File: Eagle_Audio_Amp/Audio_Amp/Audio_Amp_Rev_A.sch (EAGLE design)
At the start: 14 parts, among them IC1 LM386M-1

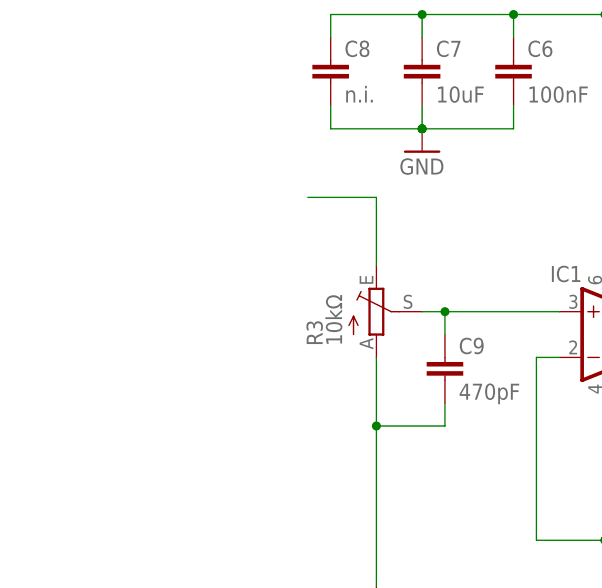
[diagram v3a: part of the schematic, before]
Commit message: Add stereo audio jack
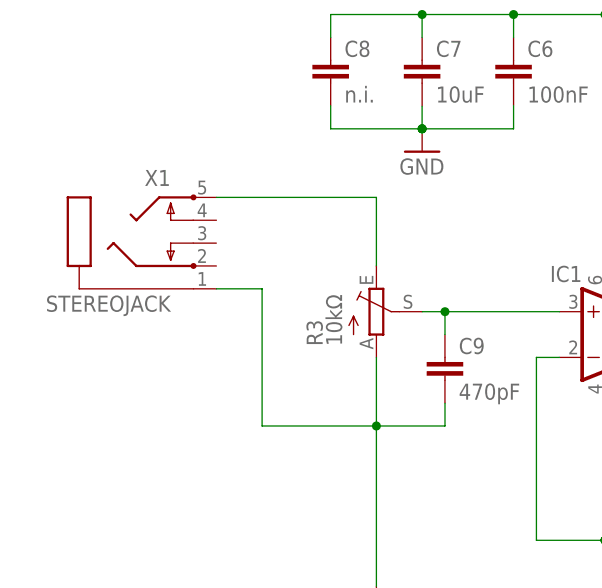
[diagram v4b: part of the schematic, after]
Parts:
- added X1: STEREOJACK, adafruit:STEREOJACK
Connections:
- net GND: now also X1.1
- net N$8: now also X1.5
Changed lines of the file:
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@@
 <layer number="48" name="Document" color="7" fill="1" visible="no" active="no"/>
 <layer number="49" name="Reference" color="7" fill="1" visible="no" active="no"/>
+<layer number="50" name="dxf" color="7" fill="1" visible="no" active="no"/>
 <layer number="51" name="tDocu" color="6" fill="1" visible="no" active="no"/>
 <layer number="52" name="bDocu" color="7" fill="1" visible="no" active="no"/>
+<layer number="53" name="tGND_GNDA" color="7" fill="9" visible="no" active="no"/>
+<layer number="54" name="bGND_GNDA" color="1" fill="9" visible="no" active="no"/>
+<layer number="56" name="wert" color="7" fill="1" visible="no" active="no"/>
+<layer number="57" name="tCAD" color="7" fill="1" visible="no" active="no"/>
+<layer number="59" name="tCarbon" color="7" fill="1" visible="no" active="no"/>
+<layer number="60" name="bCarbon" color="7" fill="1" visible="no" active="no"/>
 <layer number="90" name="Modules" color="5" fill="1" visible="yes" active="yes"/>
 <layer number="91" name="Nets" color="2" fill="1" visible="yes" active="yes"/>
@@
 <layer number="97" name="Info" color="7" fill="1" visible="yes" active="yes"/>
 <layer number="98" name="Guide" color="6" fill="1" visible="yes" active="yes"/>
+<layer number="99" name="SpiceOrder" color="7" fill="1" visible="no" active="no"/>
+<layer number="100" name="Muster" color="7" fill="1" visible="no" active="no"/>
+<layer number="101" name="Patch_Top" color="12" fill="4" visible="no" active="yes"/>
+<layer number="102" name="Vscore" color="7" fill="1" visible="no" active="yes"/>
+<layer number="103" name="fp3" color="7" fill="1" visible="no" active="yes"/>
+<layer number="104" name="Name" color="7" fill="1" visible="no" active="yes"/>
+<layer number="105" name="Beschreib" color="9" fill="1" visible="no" active="yes"/>
+<layer number="106" name="BGA-Top" color="4" fill="1" visible="no" active="yes"/>
+<layer number="107" name="BD-Top" color="5" fill="1" visible="no" active="yes"/>
+<layer number="108" name="fp8" color="7" fill="1" visible="no" active="yes"/>
+<layer number="109" name="fp9" color="7" fill="1" visible="no" active="yes"/>
+<layer number="110" name="fp0" color="7" fill="1" visible="no" active="yes"/>
+<layer number="111" name="LPC17xx" color="7" fill="1" visible="no" active="yes"/>
+<layer number="112" name="tSilk" color="7" fill="1" visible="no" active="yes"/>
+<layer number="113" name="ReferenceLS" color="7" fill="1" visible="no" active="no"/>
+<layer number="116" name="Patch_BOT" color="9" fill="4" visible="no" active="yes"/>
+<layer number="118" name="Rect_Pads" color="7" fill="1" visible="no" active="no"/>
+<layer number="121" name="_tsilk" color="7" fill="1" visible="no" active="yes"/>
+<layer number="122" name="_bsilk" color="7" fill="1" visible="no" active="yes"/>
+<layer number="123" name="tTestmark" color="7" fill="1" visible="no" active="yes"/>
+<layer number="124" name="bTestmark" color="7" fill="1" visible="no" active="yes"/>
+<layer number="125" name="_tNames" color="7" fill="1" visible="no" active="yes"/>
+<layer number="126" name="_bNames" color="7" fill="1" visible="no" active="yes"/>
+<layer number="127" name="_tValues" color="7" fill="1" visible="no" active="yes"/>
+<layer number="128" name="_bValues" color="7" fill="1" visible="no" active="yes"/>
+<layer number="129" name="Mask" color="7" fill="1" visible="yes" active="yes"/>
+<layer number="131" name="tAdjust" color="7" fill="1" visible="no" active="yes"/>
+<layer number="132" name="bAdjust" color="7" fill="1" visible="no" active="yes"/>
+<layer number="144" name="Drill_legend" color="7" fill="1" visible="no" active="yes"/>
+<layer number="150" name="Notes" color="7" fill="1" visible="no" active="yes"/>
+<layer number="151" name="HeatSink" color="7" fill="1" visible="no" active="yes"/>
+<layer number="152" name="_bDocu" color="7" fill="1" visible="no" active="yes"/>
+<layer number="153" name="FabDoc1" color="6" fill="1" visible="no" active="no"/>
+<layer number="154" name="FabDoc2" color="2" fill="1" visible="no" active="no"/>
+<layer number="155" name="FabDoc3" color="7" fill="15" visible="no" active="no"/>
+<layer number="199" name="Contour" color="7" fill="1" visible="no" active="yes"/>
+<layer number="200" name="200bmp" color="1" fill="10" visible="no" active="yes"/>
+<layer number="201" name="201bmp" color="2" fill="1" visible="no" active="no"/>
+<layer number="202" name="202bmp" color="3" fill="1" visible="no" active="no"/>
+<layer number="203" name="203bmp" color="4" fill="10" visible="no" active="yes"/>
+<layer number="204" name="204bmp" color="5" fill="10" visible="no" active="yes"/>
+<layer number="205" name="205bmp" color="6" fill="10" visible="no" active="yes"/>
+<layer number="206" name="206bmp" color="7" fill="10" visible="no" active="yes"/>
+<layer number="207" name="207bmp" color="8" fill="10" visible="no" active="yes"/>
+<layer number="208" name="208bmp" color="9" fill="10" visible="no" active="yes"/>
+<layer number="209" name="209bmp" color="7" fill="1" visible="no" active="yes"/>
+<layer number="210" name="210bmp" color="7" fill="1" visible="no" active="yes"/>
+<layer number="211" name="211bmp" color="7" fill="1" visible="no" active="yes"/>
+<layer number="212" name="212bmp" color="7" fill="1" visible="no" active="yes"/>
+<layer number="213" name="213bmp" color="7" fill="1" visible="no" active="yes"/>
+<layer number="214" name="214bmp" color="7" fill="1" visible="no" active="yes"/>
+<layer number="215" name="215bmp" color="7" fill="1" visible="no" active="yes"/>
+<layer number="216" name="216bmp" color="7" fill="1" visible="no" active="yes"/>
+<layer number="217" name="217bmp" color="18" fill="1" visible="no" active="no"/>
+<layer number="218" name="218bmp" color="19" fill="1" visible="no" active="no"/>
+<layer number="219" name="219bmp" color="20" fill="1" visible="no" active="no"/>
+<layer number="220" name="220bmp" color="21" fill="1" visible="no" active="no"/>
+<layer number="221" name="221bmp" color="22" fill="1" visible="no" active="no"/>
+<layer number="222" name="222bmp" color="23" fill="1" visible="no" active="no"/>
+<layer number="223" name="223bmp" color="24" fill="1" visible="no" active="no"/>
+<layer number="224" name="224bmp" color="25" fill="1" visible="no" active="no"/>
+<layer number="225" name="225bmp" color="7" fill="1" visible="yes" active="yes"/>
+<layer number="226" name="226bmp" color="7" fill="1" visible="yes" active="yes"/>
+<layer number="227" name="227bmp" color="7" fill="1" visible="yes" active="yes"/>
+<layer number="228" name="228bmp" color="7" fill="1" visible="yes" active="yes"/>
+<layer number="229" name="229bmp" color="7" fill="1" visible="yes" active="yes"/>
+<layer number="230" name="230bmp" color="7" fill="1" visible="yes" active="yes"/>
+<layer number="231" name="Eagle3D_PG1" color="7" fill="1" visible="no" active="no"/>
+<layer number="232" name="Eagle3D_PG2" color="7" fill="1" visible="no" active="no"/>
+<layer number="233" name="Eagle3D_PG3" color="7" fill="1" visible="no" active="no"/>
+<layer number="248" name="Housing" color="7" fill="1" visible="no" active="yes"/>
+<layer number="249" name="Edge" color="7" fill="1" visible="no" active="yes"/>
+<layer number="250" name="Descript" color="7" fill="1" visible="no" active="no"/>
+<layer number="251" name="SMDround" color="7" fill="1" visible="no" active="no"/>
+<layer number="254" name="cooling" color="7" fill="1" visible="no" active="yes"/>
+<layer number="255" name="routoute" color="7" fill="1" visible="yes" active="yes"/>
 </layers>
 <schematic xreflabel="%F%N/%S.%C%R" xrefpart="/%S.%C%R">
@@
 <part name="SP1" library="speaker" deviceset="SMS-1308MS-2-R" device=""/>
 <part name="GND5" library="supply1" deviceset="GND" device=""/>
+<part name="X1" library="adafruit" deviceset="STEREOJACK" device=""/>
 </parts>
 <sheets>
@@
 <instance part="SP1" gate="A" x="144.78" y="40.64"/>
 <instance part="GND5" gate="1" x="144.78" y="25.4"/>
+<instance part="X1" gate="1" x="33.02" y="68.58" rot="MR0"/>
 </instances>
 <busses>
@@
 <wire x1="71.12" y1="45.72" x2="63.5" y2="45.72" width="0.1524" layer="91"/>
 <junction x="63.5" y="45.72"/>
+<pinref part="X1" gate="1" pin="1"/>
+<wire x1="45.72" y1="60.96" x2="50.8" y2="60.96" width="0.1524" layer="91"/>
+<wire x1="50.8" y1="60.96" x2="50.8" y2="45.72" width="0.1524" layer="91"/>
+<wire x1="50.8" y1="45.72" x2="63.5" y2="45.72" width="0.1524" layer="91"/>
 </segment>
 <segment>
@@
 <pinref part="R3" gate="1" pin="E"/>
 <wire x1="63.5" y1="63.5" x2="63.5" y2="71.12" width="0.1524" layer="91"/>
-<wire x1="63.5" y1="71.12" x2="55.88" y2="71.12" width="0.1524" layer="91"/>
-</segment>
-</net>
+<pinref part="X1" gate="1" pin="5"/>
+<wire x1="45.72" y1="71.12" x2="63.5" y2="71.12" width="0.1524" layer="91"/>
+</segment>
+</net>

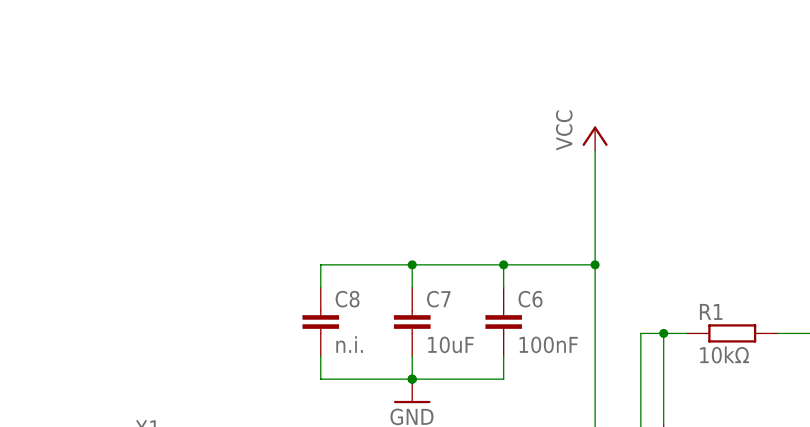
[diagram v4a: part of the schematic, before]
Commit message: Add USB micro B connector for power
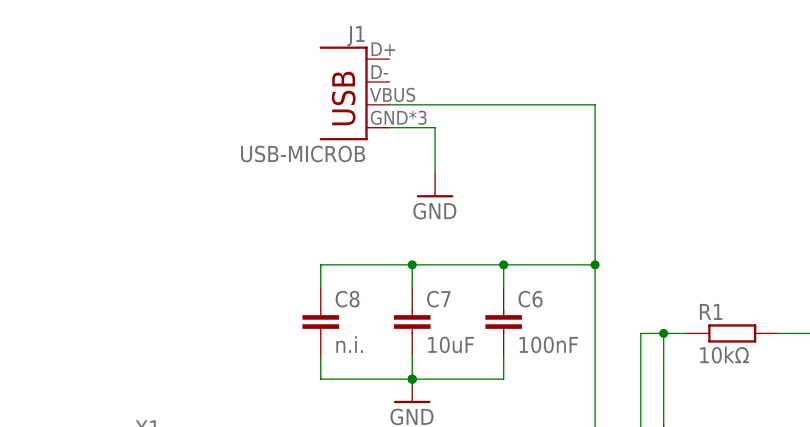
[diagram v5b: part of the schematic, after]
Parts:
- added J1: USB-MICROB, SparkFun-Connectors:USB-MICROB
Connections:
- removed net VCC: C6.1, C7.1, C8.1, IC1.VS
- new net N$10: C6.1, C7.1, C8.1, IC1.VS, J1.VBUS
- net GND: now also J1.GND
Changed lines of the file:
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@@
 <layer number="112" name="tSilk" color="7" fill="1" visible="no" active="yes"/>
 <layer number="113" name="ReferenceLS" color="7" fill="1" visible="no" active="no"/>
+<layer number="114" name="Badge_Outline" color="7" fill="1" visible="yes" active="yes"/>
+<layer number="115" name="ReferenceISLANDS" color="7" fill="1" visible="yes" active="yes"/>
 <layer number="116" name="Patch_BOT" color="9" fill="4" visible="no" active="yes"/>
 <layer number="118" name="Rect_Pads" color="7" fill="1" visible="no" active="no"/>
@@
 <part name="GND1" library="supply1" deviceset="GND" device=""/>
 <part name="GND2" library="supply1" deviceset="GND" device=""/>
-<part name="P+1" library="supply1" deviceset="VCC" device=""/>
 <part name="R3" library="pot" deviceset="TRIM_EU-" device="CIP20C-6MM" value="10kΩ"/>
 <part name="R2" library="rcl" deviceset="R-EU_" device="R0805" value="10Ω"/>
@@
 <part name="GND5" library="supply1" deviceset="GND" device=""/>
 <part name="X1" library="adafruit" deviceset="STEREOJACK" device=""/>
+<part name="J1" library="SparkFun-Connectors" deviceset="USB" device="-MICROB"/>
+<part name="GND6" library="supply1" deviceset="GND" device=""/>
 </parts>
 <sheets>
@@
 <instance part="GND1" gate="1" x="63.5" y="25.4"/>
 <instance part="GND2" gate="1" x="88.9" y="25.4"/>
-<instance part="P+1" gate="VCC" x="88.9" y="106.68"/>
 <instance part="R3" gate="1" x="63.5" y="58.42"/>
 <instance part="R2" gate="G$1" x="114.3" y="35.56" rot="R90"/>
@@
 <instance part="GND5" gate="1" x="144.78" y="25.4"/>
 <instance part="X1" gate="1" x="33.02" y="68.58" rot="MR0"/>
+<instance part="J1" gate="G$1" x="63.5" y="106.68" rot="MR0"/>
+<instance part="GND6" gate="1" x="71.12" y="99.06"/>
 </instances>
 <busses>
@@
 <pinref part="GND5" gate="1" pin="GND"/>
 </segment>
+<segment>
+<pinref part="J1" gate="G$1" pin="GND"/>
+<pinref part="GND6" gate="1" pin="GND"/>
+<wire x1="66.04" y1="106.68" x2="71.12" y2="106.68" width="0.1524" layer="91"/>
+<wire x1="71.12" y1="106.68" x2="71.12" y2="101.6" width="0.1524" layer="91"/>
+</segment>
 </net>
 <net name="N$1" class="0">
@@
 </segment>
 </net>
-<net name="VCC" class="0">
+<net name="N$8" class="0">
+<segment>
+<pinref part="R3" gate="1" pin="E"/>
+<wire x1="63.5" y1="63.5" x2="63.5" y2="71.12" width="0.1524" layer="91"/>
+<pinref part="X1" gate="1" pin="5"/>
+<wire x1="45.72" y1="71.12" x2="63.5" y2="71.12" width="0.1524" layer="91"/>
+</segment>
+</net>
+<net name="N$9" class="0">
+<segment>
+<pinref part="IC1" gate="G$1" pin="GAIN@2"/>
+<pinref part="C5" gate="G$1" pin="2"/>
+<wire x1="96.52" y1="60.96" x2="96.52" y2="66.04" width="0.1524" layer="91"/>
+</segment>
+</net>
+<net name="N$6" class="0">
+<segment>
+<pinref part="C3" gate="G$1" pin="2"/>
+<pinref part="R2" gate="G$1" pin="2"/>
+<wire x1="114.3" y1="43.18" x2="114.3" y2="40.64" width="0.1524" layer="91"/>
+</segment>
+</net>
+<net name="N$7" class="0">
+<segment>
+<pinref part="C4" gate="G$1" pin="2"/>
+<wire x1="132.08" y1="55.88" x2="144.78" y2="55.88" width="0.1524" layer="91"/>
+<pinref part="SP1" gate="A" pin="1"/>
+<wire x1="144.78" y1="55.88" x2="144.78" y2="45.72" width="0.1524" layer="91"/>
+</segment>
+</net>
+<net name="N$10" class="0">
 <segment>
 <pinref part="IC1" gate="G$1" pin="VS"/>
-<pinref part="P+1" gate="VCC" pin="VCC"/>
 <wire x1="88.9" y1="63.5" x2="88.9" y2="91.44" width="0.1524" layer="91"/>
 <pinref part="C6" gate="G$1" pin="1"/>
-<wire x1="88.9" y1="91.44" x2="88.9" y2="104.14" width="0.1524" layer="91"/>
+<wire x1="88.9" y1="91.44" x2="88.9" y2="109.22" width="0.1524" layer="91"/>
 <wire x1="88.9" y1="91.44" x2="78.74" y2="91.44" width="0.1524" layer="91"/>
 <wire x1="78.74" y1="91.44" x2="78.74" y2="88.9" width="0.1524" layer="91"/>
@@
 <wire x1="68.58" y1="91.44" x2="68.58" y2="88.9" width="0.1524" layer="91"/>
 <junction x="68.58" y="91.44"/>
-</segment>
-</net>
-<net name="N$8" class="0">
-<segment>
-<pinref part="R3" gate="1" pin="E"/>
-<wire x1="63.5" y1="63.5" x2="63.5" y2="71.12" width="0.1524" layer="91"/>
-<pinref part="X1" gate="1" pin="5"/>
-<wire x1="45.72" y1="71.12" x2="63.5" y2="71.12" width="0.1524" layer="91"/>
-</segment>
-</net>
-<net name="N$9" class="0">
-<segment>
-<pinref part="IC1" gate="G$1" pin="GAIN@2"/>
-<pinref part="C5" gate="G$1" pin="2"/>
-<wire x1="96.52" y1="60.96" x2="96.52" y2="66.04" width="0.1524" layer="91"/>
-</segment>
-</net>
-<net name="N$6" class="0">
-<segment>
-<pinref part="C3" gate="G$1" pin="2"/>
-<pinref part="R2" gate="G$1" pin="2"/>
-<wire x1="114.3" y1="43.18" x2="114.3" y2="40.64" width="0.1524" layer="91"/>
-</segment>
-</net>
-<net name="N$7" class="0">
-<segment>
-<pinref part="C4" gate="G$1" pin="2"/>
-<wire x1="132.08" y1="55.88" x2="144.78" y2="55.88" width="0.1524" layer="91"/>
-<pinref part="SP1" gate="A" pin="1"/>
-<wire x1="144.78" y1="55.88" x2="144.78" y2="45.72" width="0.1524" layer="91"/>
-</segment>
-</net>
+<pinref part="J1" gate="G$1" pin="VBUS"/>
+<wire x1="66.04" y1="109.22" x2="88.9" y2="109.22" width="0.1524" layer="91"/>
+</segment>
+</net>

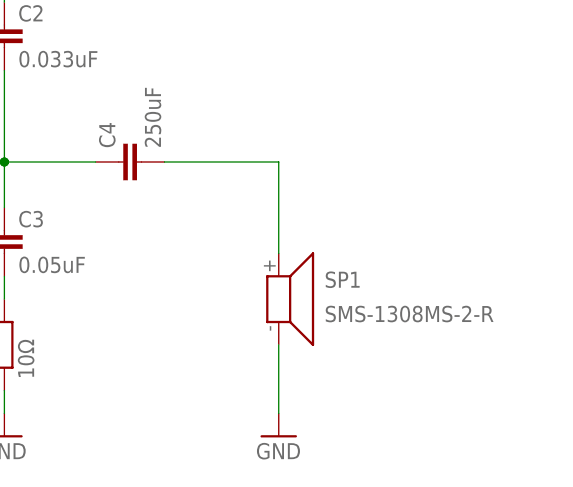
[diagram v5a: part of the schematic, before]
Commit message: Replace speaker with 2 pin header
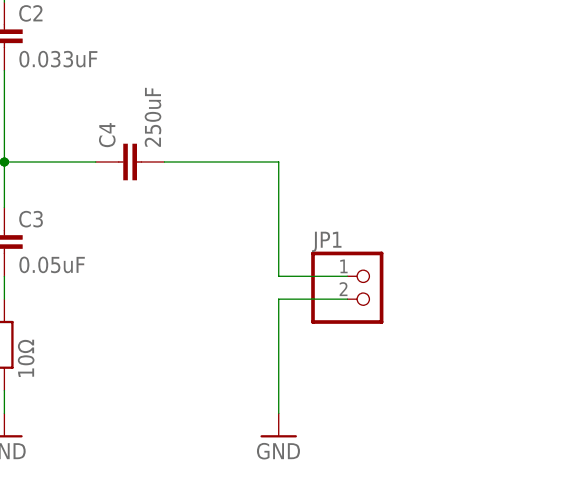
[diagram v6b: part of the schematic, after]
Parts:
- removed SP1: SMS-1308MS-2-R, speaker:SMS-1308MS-2-R
- added JP1: (no value), pinhead:PINHD-1X2
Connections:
- net GND: now also JP1.2; no longer SP1.2
- net N$7: now also JP1.1; no longer SP1.1
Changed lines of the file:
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@@
 <part name="C8" library="rcl" deviceset="C-EU" device="C0805" value="n.i."/>
 <part name="C9" library="rcl" deviceset="C-EU" device="C0805" value="470pF"/>
-<part name="SP1" library="speaker" deviceset="SMS-1308MS-2-R" device=""/>
 <part name="GND5" library="supply1" deviceset="GND" device=""/>
 <part name="X1" library="adafruit" deviceset="STEREOJACK" device=""/>
 <part name="J1" library="SparkFun-Connectors" deviceset="USB" device="-MICROB"/>
 <part name="GND6" library="supply1" deviceset="GND" device=""/>
+<part name="JP1" library="pinhead" deviceset="PINHD-1X2" device=""/>
 </parts>
 <sheets>
@@
 <instance part="C8" gate="G$1" x="58.42" y="86.36"/>
 <instance part="C9" gate="G$1" x="71.12" y="53.34"/>
-<instance part="SP1" gate="A" x="144.78" y="40.64"/>
 <instance part="GND5" gate="1" x="144.78" y="25.4"/>
 <instance part="X1" gate="1" x="33.02" y="68.58" rot="MR0"/>
 <instance part="J1" gate="G$1" x="63.5" y="106.68" rot="MR0"/>
 <instance part="GND6" gate="1" x="71.12" y="99.06"/>
+<instance part="JP1" gate="G$1" x="154.94" y="40.64"/>
 </instances>
 <busses>
@@
 </segment>
 <segment>
-<pinref part="SP1" gate="A" pin="2"/>
-<wire x1="144.78" y1="35.56" x2="144.78" y2="27.94" width="0.1524" layer="91"/>
+<wire x1="144.78" y1="40.64" x2="144.78" y2="27.94" width="0.1524" layer="91"/>
 <pinref part="GND5" gate="1" pin="GND"/>
+<pinref part="JP1" gate="G$1" pin="2"/>
+<wire x1="144.78" y1="40.64" x2="152.4" y2="40.64" width="0.1524" layer="91"/>
 </segment>
 <segment>
@@
 <pinref part="C4" gate="G$1" pin="2"/>
 <wire x1="132.08" y1="55.88" x2="144.78" y2="55.88" width="0.1524" layer="91"/>
-<pinref part="SP1" gate="A" pin="1"/>
-<wire x1="144.78" y1="55.88" x2="144.78" y2="45.72" width="0.1524" layer="91"/>
+<wire x1="144.78" y1="55.88" x2="144.78" y2="43.18" width="0.1524" layer="91"/>
+<pinref part="JP1" gate="G$1" pin="1"/>
+<wire x1="144.78" y1="43.18" x2="152.4" y2="43.18" width="0.1524" layer="91"/>
 </segment>
 </net>
